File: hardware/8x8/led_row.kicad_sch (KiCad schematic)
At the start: 8 parts

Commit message: Updated Pin Headers
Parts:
- LED_1: renamed from LED_0; value (none) -> WP154A4SEJ3VBDZGC/CA
- LED_2: renamed from LED_1; value (none) -> WP154A4SEJ3VBDZGC/CA
- LED_3: renamed from LED_2; value (none) -> WP154A4SEJ3VBDZGC/CA
- LED_4: renamed from LED_3; value (none) -> WP154A4SEJ3VBDZGC/CA
- LED_5: renamed from LED_4; value (none) -> WP154A4SEJ3VBDZGC/CA
- LED_6: renamed from LED_5; value (none) -> WP154A4SEJ3VBDZGC/CA
- LED_7: renamed from LED_6; value (none) -> WP154A4SEJ3VBDZGC/CA
- LED_8: renamed from LED_7; value (none) -> WP154A4SEJ3VBDZGC/CA
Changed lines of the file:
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@@
   (symbol (lib_id "RGB LED:WP154A4SEJ3VBDZGC{brace}slash}CA") (at 25.4 50.8 0) (unit 1)
     (in_bom yes) (on_board yes) (fields_autoplaced)
-    (property "Reference" "LED_0" (id 0) (at 33.02 35.56 0)
+    (property "Reference" "LED_1" (id 0) (at 33.02 35.56 0)
       (effects (font (size 1.524 1.524)))
     )
-    (property "Value" "" (id 1) (at 33.02 35.56 0)
+    (property "Value" "WP154A4SEJ3VBDZGC{slash}CA" (id 1) (at 33.02 35.56 0)
       (effects (font (size 1.524 1.524)) hide)
     )
@@
   (symbol (lib_id "RGB LED:WP154A4SEJ3VBDZGC{brace}slash}CA") (at 76.2 50.8 0) (unit 1)
     (in_bom yes) (on_board yes) (fields_autoplaced)
-    (property "Reference" "LED_2" (id 0) (at 83.82 35.56 0)
+    (property "Reference" "LED_3" (id 0) (at 83.82 35.56 0)
       (effects (font (size 1.524 1.524)))
     )
-    (property "Value" "" (id 1) (at 83.82 35.56 0)
+    (property "Value" "WP154A4SEJ3VBDZGC{slash}CA" (id 1) (at 83.82 35.56 0)
       (effects (font (size 1.524 1.524)) hide)
     )
@@
   (symbol (lib_id "RGB LED:WP154A4SEJ3VBDZGC{brace}slash}CA") (at 177.8 50.8 0) (unit 1)
     (in_bom yes) (on_board yes) (fields_autoplaced)
-    (property "Reference" "LED_6" (id 0) (at 185.42 35.56 0)
+    (property "Reference" "LED_7" (id 0) (at 185.42 35.56 0)
       (effects (font (size 1.524 1.524)))
     )
-    (property "Value" "" (id 1) (at 185.42 35.56 0)
+    (property "Value" "WP154A4SEJ3VBDZGC{slash}CA" (id 1) (at 185.42 35.56 0)
       (effects (font (size 1.524 1.524)) hide)
     )
@@
   (symbol (lib_id "RGB LED:WP154A4SEJ3VBDZGC{brace}slash}CA") (at 50.8 50.8 0) (unit 1)
     (in_bom yes) (on_board yes) (fields_autoplaced)
-    (property "Reference" "LED_1" (id 0) (at 58.42 35.56 0)
+    (property "Reference" "LED_2" (id 0) (at 58.42 35.56 0)
       (effects (font (size 1.524 1.524)))
     )
-    (property "Value" "" (id 1) (at 58.42 35.56 0)
+    (property "Value" "WP154A4SEJ3VBDZGC{slash}CA" (id 1) (at 58.42 35.56 0)
       (effects (font (size 1.524 1.524)) hide)
     )
@@
   (symbol (lib_id "RGB LED:WP154A4SEJ3VBDZGC{brace}slash}CA") (at 127 50.8 0) (unit 1)
     (in_bom yes) (on_board yes) (fields_autoplaced)
-    (property "Reference" "LED_4" (id 0) (at 134.62 35.56 0)
+    (property "Reference" "LED_5" (id 0) (at 134.62 35.56 0)
       (effects (font (size 1.524 1.524)))
     )
-    (property "Value" "" (id 1) (at 134.62 35.56 0)
+    (property "Value" "WP154A4SEJ3VBDZGC{slash}CA" (id 1) (at 134.62 35.56 0)
       (effects (font (size 1.524 1.524)) hide)
     )
@@
   (symbol (lib_id "RGB LED:WP154A4SEJ3VBDZGC{brace}slash}CA") (at 101.6 50.8 0) (unit 1)
     (in_bom yes) (on_board yes) (fields_autoplaced)
-    (property "Reference" "LED_3" (id 0) (at 109.22 35.56 0)
+    (property "Reference" "LED_4" (id 0) (at 109.22 35.56 0)
       (effects (font (size 1.524 1.524)))
     )
-    (property "Value" "" (id 1) (at 109.22 35.56 0)
+    (property "Value" "WP154A4SEJ3VBDZGC{slash}CA" (id 1) (at 109.22 35.56 0)
       (effects (font (size 1.524 1.524)) hide)
     )
@@
   (symbol (lib_id "RGB LED:WP154A4SEJ3VBDZGC{brace}slash}CA") (at 203.2 50.8 0) (unit 1)
     (in_bom yes) (on_board yes) (fields_autoplaced)
-    (property "Reference" "LED_7" (id 0) (at 210.82 35.56 0)
+    (property "Reference" "LED_8" (id 0) (at 210.82 35.56 0)
       (effects (font (size 1.524 1.524)))
     )
-    (property "Value" "" (id 1) (at 210.82 35.56 0)
+    (property "Value" "WP154A4SEJ3VBDZGC{slash}CA" (id 1) (at 210.82 35.56 0)
       (effects (font (size 1.524 1.524)) hide)
     )
@@
   (symbol (lib_id "RGB LED:WP154A4SEJ3VBDZGC{brace}slash}CA") (at 152.4 50.8 0) (unit 1)
     (in_bom yes) (on_board yes) (fields_autoplaced)
-    (property "Reference" "LED_5" (id 0) (at 160.02 35.56 0)
+    (property "Reference" "LED_6" (id 0) (at 160.02 35.56 0)
       (effects (font (size 1.524 1.524)))
     )
-    (property "Value" "" (id 1) (at 160.02 35.56 0)
+    (property "Value" "WP154A4SEJ3VBDZGC{slash}CA" (id 1) (at 160.02 35.56 0)
       (effects (font (size 1.524 1.524)) hide)
     )

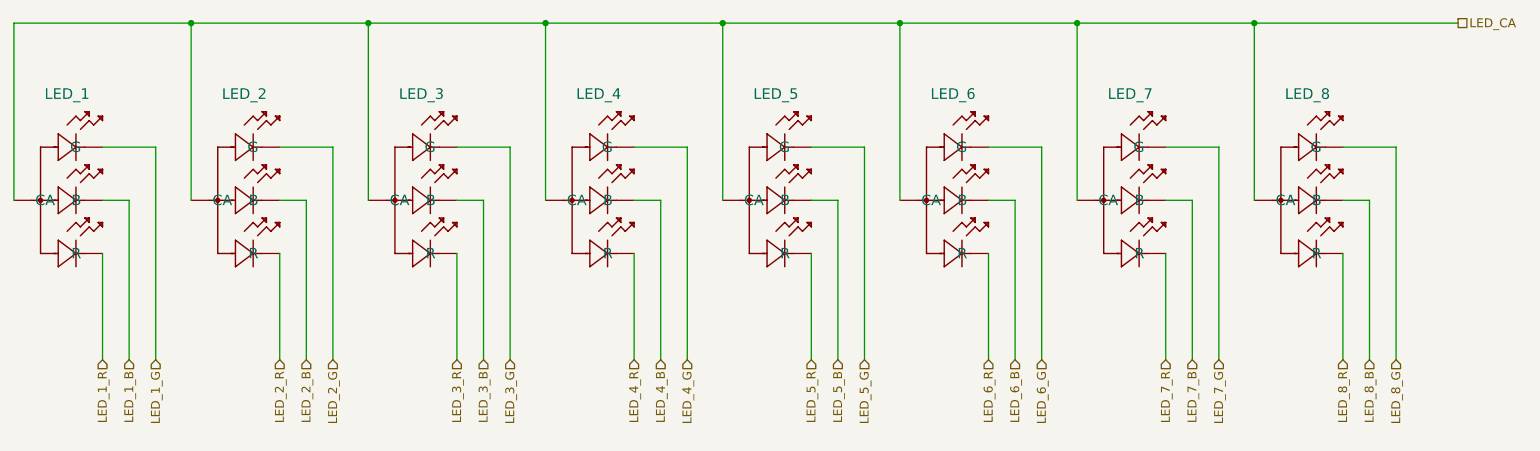
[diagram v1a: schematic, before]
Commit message: Temporary Component Placement on PCB
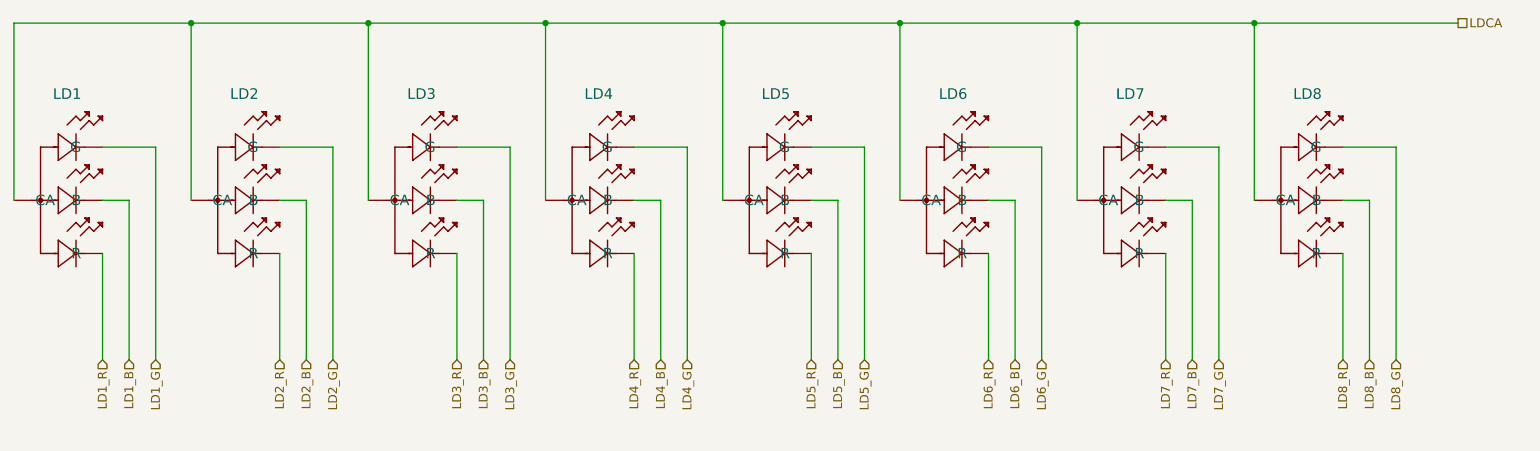
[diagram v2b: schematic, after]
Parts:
- renumbered LED_1 to LD1, LED_2 to LD2, LED_3 to LD3, LED_4 to LD4, LED_5 to LD5, LED_6 to LD6, LED_7 to LD7, LED_8 to LD8
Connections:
- net LED_1_B renamed LD1_B
- net LED_1_G renamed LD1_G
- net LED_1_R renamed LD1_R
- net LED_2_B renamed LD2_B
- net LED_2_G renamed LD2_G
- net LED_2_R renamed LD2_R
- net LED_3_B renamed LD3_B
- net LED_3_G renamed LD3_G
- net LED_3_R renamed LD3_R
- net LED_4_B renamed LD4_B
- net LED_4_G renamed LD4_G
- net LED_4_R renamed LD4_R
- net LED_5_B renamed LD5_B
- net LED_5_G renamed LD5_G
- net LED_5_R renamed LD5_R
- net LED_6_B renamed LD6_B
- net LED_6_G renamed LD6_G
- net LED_6_R renamed LD6_R
- net LED_7_B renamed LD7_B
- net LED_7_G renamed LD7_G
- net LED_7_R renamed LD7_R
- net LED_8_B renamed LD8_B
- net LED_8_G renamed LD8_G
- net LED_8_R renamed LD8_R
- net LED_CA renamed LDCA
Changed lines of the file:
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@@
     (stroke (width 0) (type default) (color 0 0 0 0))
   )
-  (hierarchical_label "LED_1_G" (shape input) (at 45.72 73.66 270)
-    (effects (font (size 1.27 1.27)) (justify right))
-  )
-  (hierarchical_label "LED_7_R" (shape input) (at 190.5 73.66 270)
-    (effects (font (size 1.27 1.27)) (justify right))
-  )
-  (hierarchical_label "LED_6_G" (shape input) (at 172.72 73.66 270)
-    (effects (font (size 1.27 1.27)) (justify right))
-  )
-  (hierarchical_label "LED_5_R" (shape input) (at 139.7 73.66 270)
-    (effects (font (size 1.27 1.27)) (justify right))
-  )
-  (hierarchical_label "LED_4_G" (shape input) (at 121.92 73.66 270)
-    (effects (font (size 1.27 1.27)) (justify right))
-  )
-  (hierarchical_label "LED_7_B" (shape input) (at 194.31 73.66 270)
-    (effects (font (size 1.27 1.27)) (justify right))
-  )
-  (hierarchical_label "LED_6_R" (shape input) (at 165.1 73.66 270)
-    (effects (font (size 1.27 1.27)) (justify right))
-  )
-  (hierarchical_label "LED_2_G" (shape input) (at 71.12 73.66 270)
-    (effects (font (size 1.27 1.27)) (justify right))
-  )
-  (hierarchical_label "LED_3_B" (shape input) (at 92.71 73.66 270)
-    (effects (font (size 1.27 1.27)) (justify right))
-  )
-  (hierarchical_label "LED_2_R" (shape input) (at 63.5 73.66 270)
-    (effects (font (size 1.27 1.27)) (justify right))
-  )
-  (hierarchical_label "LED_8_G" (shape input) (at 223.52 73.66 270)
-    (effects (font (size 1.27 1.27)) (justify right))
-  )
-  (hierarchical_label "LED_6_B" (shape input) (at 168.91 73.66 270)
-    (effects (font (size 1.27 1.27)) (justify right))
-  )
-  (hierarchical_label "LED_2_B" (shape input) (at 67.31 73.66 270)
-    (effects (font (size 1.27 1.27)) (justify right))
-  )
-  (hierarchical_label "LED_5_B" (shape input) (at 143.51 73.66 270)
-    (effects (font (size 1.27 1.27)) (justify right))
-  )
-  (hierarchical_label "LED_5_G" (shape input) (at 147.32 73.66 270)
-    (effects (font (size 1.27 1.27)) (justify right))
-  )
-  (hierarchical_label "LED_3_R" (shape input) (at 88.9 73.66 270)
-    (effects (font (size 1.27 1.27)) (justify right))
-  )
-  (hierarchical_label "LED_1_R" (shape input) (at 38.1 73.66 270)
-    (effects (font (size 1.27 1.27)) (justify right))
-  )
-  (hierarchical_label "LED_4_R" (shape input) (at 114.3 73.66 270)
-    (effects (font (size 1.27 1.27)) (justify right))
-  )
-  (hierarchical_label "LED_7_G" (shape input) (at 198.12 73.66 270)
-    (effects (font (size 1.27 1.27)) (justify right))
-  )
-  (hierarchical_label "LED_8_R" (shape input) (at 215.9 73.66 270)
-    (effects (font (size 1.27 1.27)) (justify right))
-  )
-  (hierarchical_label "LED_3_G" (shape input) (at 96.52 73.66 270)
-    (effects (font (size 1.27 1.27)) (justify right))
-  )
-  (hierarchical_label "LED_8_B" (shape input) (at 219.71 73.66 270)
-    (effects (font (size 1.27 1.27)) (justify right))
-  )
-  (hierarchical_label "LED_4_B" (shape input) (at 118.11 73.66 270)
-    (effects (font (size 1.27 1.27)) (justify right))
-  )
-  (hierarchical_label "LED_1_B" (shape input) (at 41.91 73.66 270)
-    (effects (font (size 1.27 1.27)) (justify right))
-  )
-  (hierarchical_label "LED_CA" (shape passive) (at 232.41 25.4 0)
+  (hierarchical_label "LD1_G" (shape input) (at 45.72 73.66 270)
+    (effects (font (size 1.27 1.27)) (justify right))
+  )
+  (hierarchical_label "LD7_R" (shape input) (at 190.5 73.66 270)
+    (effects (font (size 1.27 1.27)) (justify right))
+  )
+  (hierarchical_label "LD6_G" (shape input) (at 172.72 73.66 270)
+    (effects (font (size 1.27 1.27)) (justify right))
+  )
+  (hierarchical_label "LD5_R" (shape input) (at 139.7 73.66 270)
+    (effects (font (size 1.27 1.27)) (justify right))
+  )
+  (hierarchical_label "LD4_G" (shape input) (at 121.92 73.66 270)
+    (effects (font (size 1.27 1.27)) (justify right))
+  )
+  (hierarchical_label "LD7_B" (shape input) (at 194.31 73.66 270)
+    (effects (font (size 1.27 1.27)) (justify right))
+  )
+  (hierarchical_label "LD6_R" (shape input) (at 165.1 73.66 270)
+    (effects (font (size 1.27 1.27)) (justify right))
+  )
+  (hierarchical_label "LD2_G" (shape input) (at 71.12 73.66 270)
+    (effects (font (size 1.27 1.27)) (justify right))
+  )
+  (hierarchical_label "LD3_B" (shape input) (at 92.71 73.66 270)
+    (effects (font (size 1.27 1.27)) (justify right))
+  )
+  (hierarchical_label "LD2_R" (shape input) (at 63.5 73.66 270)
+    (effects (font (size 1.27 1.27)) (justify right))
+  )
+  (hierarchical_label "LD8_G" (shape input) (at 223.52 73.66 270)
+    (effects (font (size 1.27 1.27)) (justify right))
+  )
+  (hierarchical_label "LD6_B" (shape input) (at 168.91 73.66 270)
+    (effects (font (size 1.27 1.27)) (justify right))
+  )
+  (hierarchical_label "LD2_B" (shape input) (at 67.31 73.66 270)
+    (effects (font (size 1.27 1.27)) (justify right))
+  )
+  (hierarchical_label "LD5_B" (shape input) (at 143.51 73.66 270)
+    (effects (font (size 1.27 1.27)) (justify right))
+  )
+  (hierarchical_label "LD5_G" (shape input) (at 147.32 73.66 270)
+    (effects (font (size 1.27 1.27)) (justify right))
+  )
+  (hierarchical_label "LD3_R" (shape input) (at 88.9 73.66 270)
+    (effects (font (size 1.27 1.27)) (justify right))
+  )
+  (hierarchical_label "LD1_R" (shape input) (at 38.1 73.66 270)
+    (effects (font (size 1.27 1.27)) (justify right))
+  )
+  (hierarchical_label "LD4_R" (shape input) (at 114.3 73.66 270)
+    (effects (font (size 1.27 1.27)) (justify right))
+  )
+  (hierarchical_label "LD7_G" (shape input) (at 198.12 73.66 270)
+    (effects (font (size 1.27 1.27)) (justify right))
+  )
+  (hierarchical_label "LD8_R" (shape input) (at 215.9 73.66 270)
+    (effects (font (size 1.27 1.27)) (justify right))
+  )
+  (hierarchical_label "LD3_G" (shape input) (at 96.52 73.66 270)
+    (effects (font (size 1.27 1.27)) (justify right))
+  )
+  (hierarchical_label "LD8_B" (shape input) (at 219.71 73.66 270)
+    (effects (font (size 1.27 1.27)) (justify right))
+  )
+  (hierarchical_label "LD4_B" (shape input) (at 118.11 73.66 270)
+    (effects (font (size 1.27 1.27)) (justify right))
+  )
+  (hierarchical_label "LD1_B" (shape input) (at 41.91 73.66 270)
+    (effects (font (size 1.27 1.27)) (justify right))
+  )
+  (hierarchical_label "LDCA" (shape passive) (at 232.41 25.4 0)
     (effects (font (size 1.27 1.27)) (justify left))
   )
   (symbol (lib_id "RGB LED:WP154A4SEJ3VBDZGC{brace}slash}CA") (at 25.4 50.8 0) (unit 1)
     (in_bom yes) (on_board yes) (fields_autoplaced)
-    (property "Reference" "LED_1" (id 0) (at 33.02 35.56 0)
+    (property "Reference" "LD1" (id 0) (at 33.02 35.56 0)
       (effects (font (size 1.524 1.524)))
     )
@@
   (symbol (lib_id "RGB LED:WP154A4SEJ3VBDZGC{brace}slash}CA") (at 76.2 50.8 0) (unit 1)
     (in_bom yes) (on_board yes) (fields_autoplaced)
-    (property "Reference" "LED_3" (id 0) (at 83.82 35.56 0)
+    (property "Reference" "LD3" (id 0) (at 83.82 35.56 0)
       (effects (font (size 1.524 1.524)))
     )
@@
   (symbol (lib_id "RGB LED:WP154A4SEJ3VBDZGC{brace}slash}CA") (at 177.8 50.8 0) (unit 1)
     (in_bom yes) (on_board yes) (fields_autoplaced)
-    (property "Reference" "LED_7" (id 0) (at 185.42 35.56 0)
+    (property "Reference" "LD7" (id 0) (at 185.42 35.56 0)
       (effects (font (size 1.524 1.524)))
     )
@@
   (symbol (lib_id "RGB LED:WP154A4SEJ3VBDZGC{brace}slash}CA") (at 50.8 50.8 0) (unit 1)
     (in_bom yes) (on_board yes) (fields_autoplaced)
-    (property "Reference" "LED_2" (id 0) (at 58.42 35.56 0)
+    (property "Reference" "LD2" (id 0) (at 58.42 35.56 0)
       (effects (font (size 1.524 1.524)))
     )
@@
   (symbol (lib_id "RGB LED:WP154A4SEJ3VBDZGC{brace}slash}CA") (at 127 50.8 0) (unit 1)
     (in_bom yes) (on_board yes) (fields_autoplaced)
-    (property "Reference" "LED_5" (id 0) (at 134.62 35.56 0)
+    (property "Reference" "LD5" (id 0) (at 134.62 35.56 0)
       (effects (font (size 1.524 1.524)))
     )
@@
   (symbol (lib_id "RGB LED:WP154A4SEJ3VBDZGC{brace}slash}CA") (at 101.6 50.8 0) (unit 1)
     (in_bom yes) (on_board yes) (fields_autoplaced)
-    (property "Reference" "LED_4" (id 0) (at 109.22 35.56 0)
+    (property "Reference" "LD4" (id 0) (at 109.22 35.56 0)
       (effects (font (size 1.524 1.524)))
     )
@@
   (symbol (lib_id "RGB LED:WP154A4SEJ3VBDZGC{brace}slash}CA") (at 203.2 50.8 0) (unit 1)
     (in_bom yes) (on_board yes) (fields_autoplaced)
-    (property "Reference" "LED_8" (id 0) (at 210.82 35.56 0)
+    (property "Reference" "LD8" (id 0) (at 210.82 35.56 0)
       (effects (font (size 1.524 1.524)))
     )
@@
   (symbol (lib_id "RGB LED:WP154A4SEJ3VBDZGC{brace}slash}CA") (at 152.4 50.8 0) (unit 1)
     (in_bom yes) (on_board yes) (fields_autoplaced)
-    (property "Reference" "LED_6" (id 0) (at 160.02 35.56 0)
-      (effects (font (size 1.524 1.524)))
-    )
+    (property "Reference" "LD6" (id 0) (at 160.02 35.56 0)
+      (effects (font (size 1.524 1.524)))
+    )
